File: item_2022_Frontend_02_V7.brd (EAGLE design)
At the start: 160 x 100 mm, 36 parts, among them K1 351, U3 SSD1306_128X64, X1 MSTBA2, X10 MSTBA2, X11 MSTBA2, X12 MSTBA2, X13 MSTBA2, X14 MSTBA2, X15 MSTBA2, X2 MSTBA2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

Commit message: FrontEnd con PE
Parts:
- added H1, H2: MOUNT-PAD-ROUND3.6, holes:3,6-PAD
- X6, X7: value MSTBA2 -> MSTBA3; device con-phoenix-508:MSTBA2 -> con-phoenix-508:MSTBA3
- moved R1 6.16 mm to (135.9, 21.0), turned to 180 degrees
- moved X15 5.08 mm to (144.8, 95.4)
- moved X7 3.56 mm to (129.9, 95.4)
- moved D2 3.18 mm to (41.3, 73.7)
- moved D5 3.18 mm to (41.3, 66.7)
- moved X21 2.67 mm to (92.6, 95.4)
- moved X8 1.66 mm to (70.1, 95.4)
- moved X6 1.16 mm to (112.5, 95.4)
- moved X2 0.66 mm to (52.7, 95.4)
- moved X5 0.54 mm to (15.7, 95.4)
- moved X3 0.32 mm to (40.4, 95.4)
- moved X4 0.23 mm to (28.1, 95.4)
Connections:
- new net PE: H1.B3,6, H2.B3,6, X6.3, X7.3
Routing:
- net PE: track 0.00 -> 152.9 mm
- net SPEED2+: track 114.2 -> 95.5 mm, vias 1 -> 0
- net +3V3: track 160.2 -> 171.1 mm
- net EXT_+5V: track 118.9 -> 109.4 mm
- net ACCEL0+: track 106.5 -> 114.7 mm, vias 0 -> 1
- net ACCEL1+: track 106.5 -> 113.1 mm
- net I2C_SCL: track 59.6 -> 64.2 mm, vias 1 -> 0
- net TORQUE2+: track 101.6 -> 105.7 mm, vias 1 -> 0
- net SPEED1+: track 96.0 -> 99.1 mm
- net ACCEL1-: track 94.6 -> 97.3 mm
- net N$5: track 26.3 -> 28.6 mm
- net TORQUE1+: track 94.3 -> 92.9 mm, vias 1 -> 0
- net N$1: track 11.5 -> 12.4 mm
- net GND: track 351.1 -> 352.0 mm, vias 5 -> 15
- net RTD2_IN+: track 67.2 -> 66.3 mm
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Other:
- board text added: "PE"

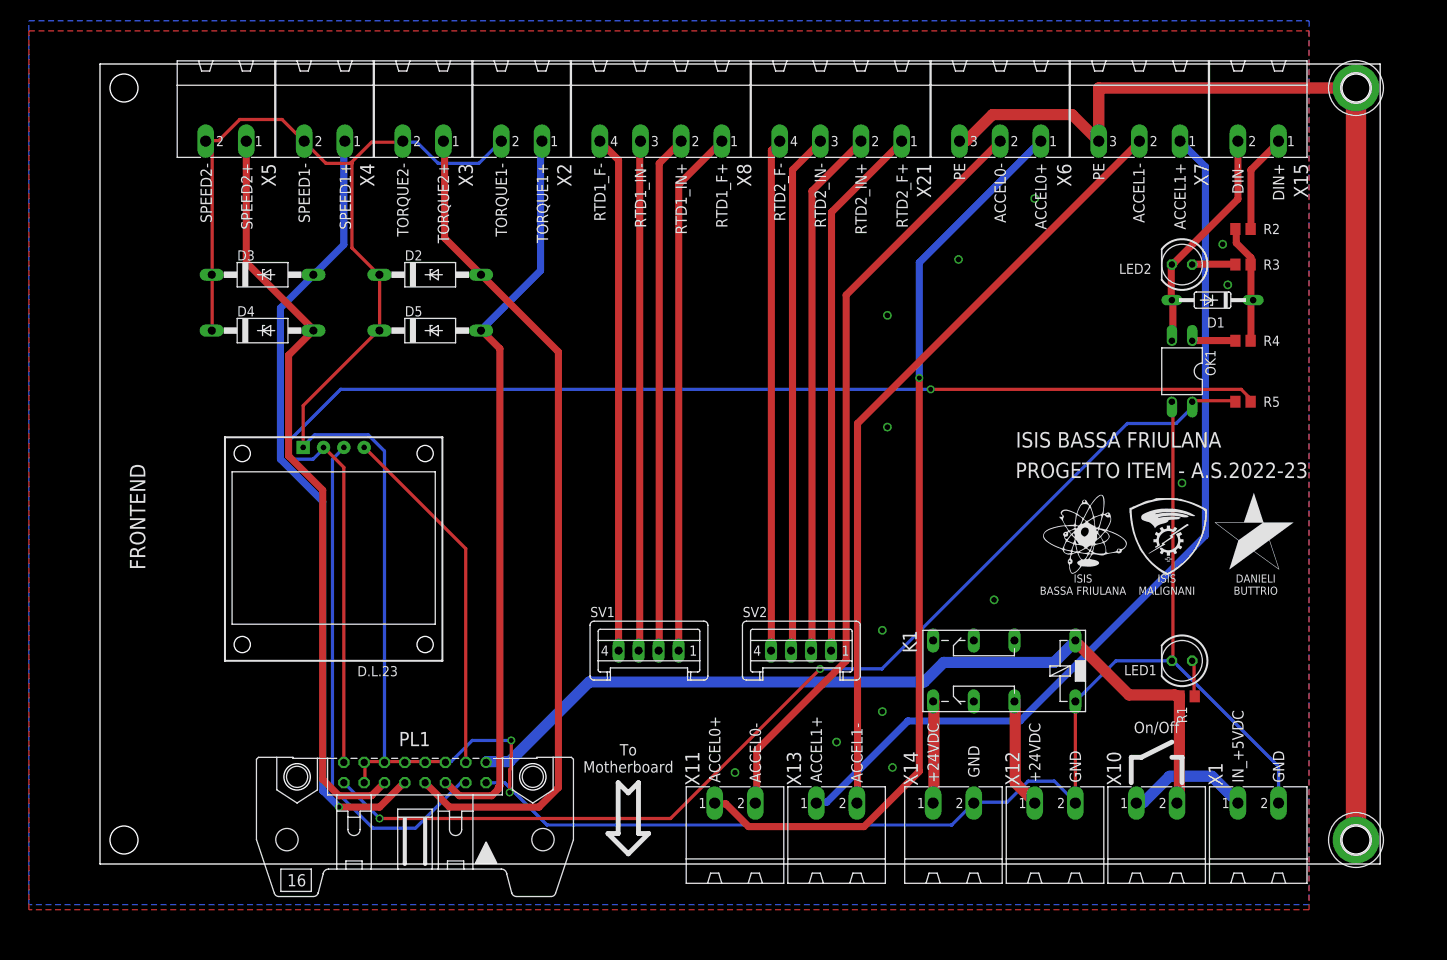
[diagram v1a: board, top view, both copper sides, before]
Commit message: corretto diametro SSD1306 e RTD
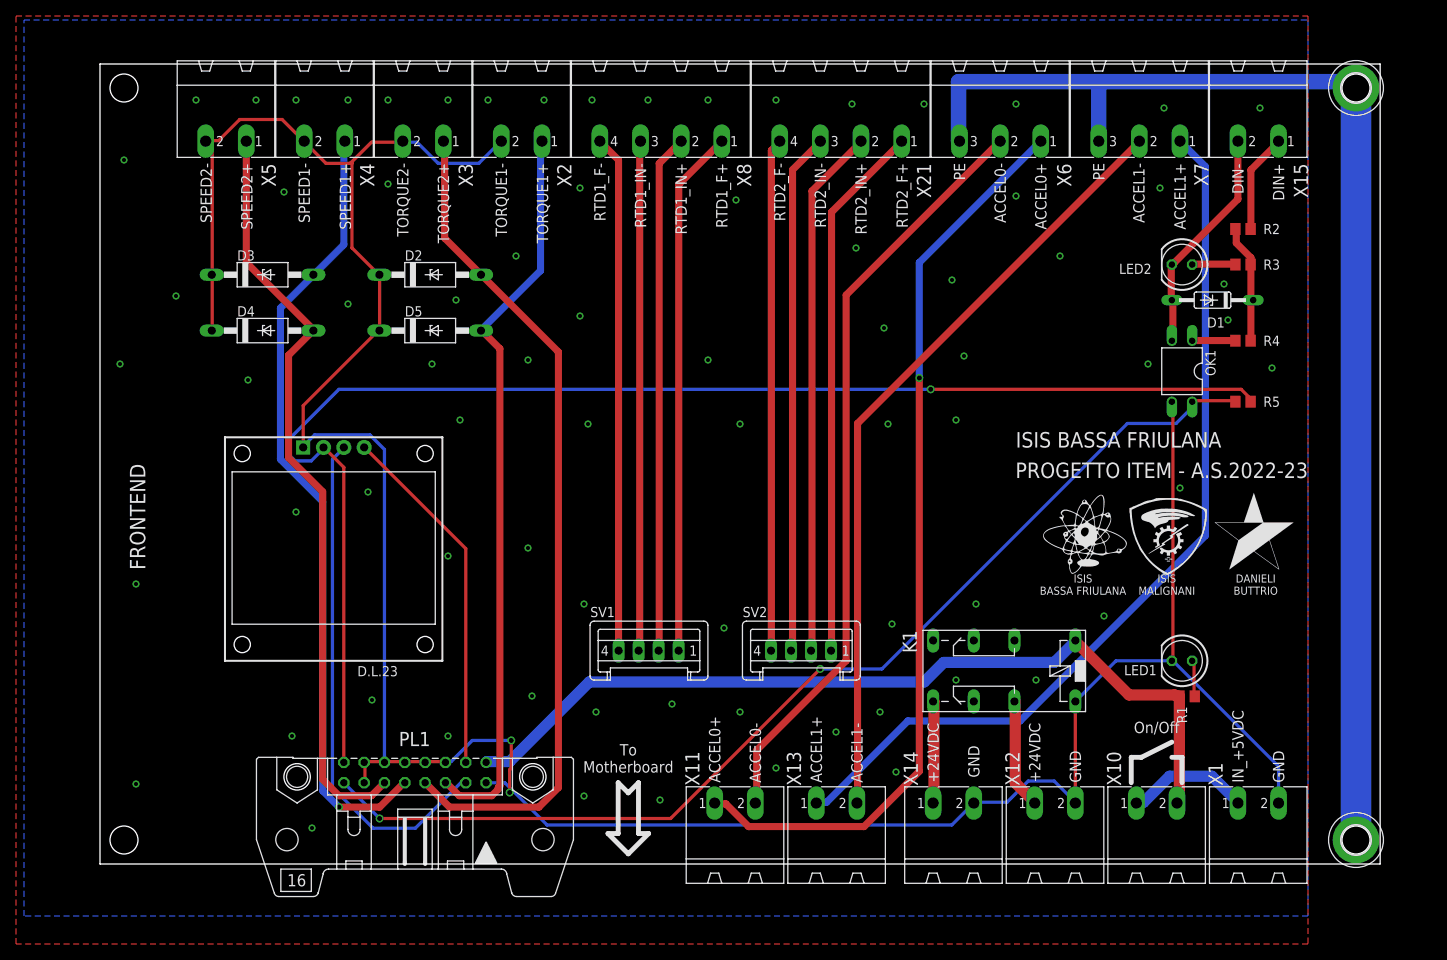
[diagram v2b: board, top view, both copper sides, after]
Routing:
- net PE: track 152.9 -> 160.1 mm
- net GND: track 352.0 -> 352.1 mm, vias 15 -> 78
